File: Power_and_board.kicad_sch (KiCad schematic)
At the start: 24 parts, among them U4 AMS1117-5.0, U5 AMS1117-3.3

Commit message: initial rev of design
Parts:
- added C15, C16: 10uF, Capacitor_SMD:C_0805_2012Metric_Pad1.18x1.45mm_HandSolder, symbol Device:C
- added D6: SMF5V0A, Diode_SMD:D_SMF, symbol Diode:SMF5V0A
- added D7, D8: 1N5819WS, Diode_SMD:D_SOD-323_HandSoldering, symbol Device:D_Schottky
- C10, C7: LCSC (none) -> C49678
- C11, C5, C6, C8, C9: LCSC (none) -> C15850
- U4: LCSC (none) -> C6187
- U5: LCSC (none) -> C6186
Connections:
- net 12VDC IN: now also C15.1, D7.1 (K)
- net 3.3V: now also D8.2 (A)
- net Earth: now also C15.2, C16.2, D6.2 (A2)
- net VDD_5V: now also C16.1, D6.1 (A1), D7.2 (A), D8.1 (K)
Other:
- moved on the sheet: C10, C11, C5, C6, C7, C8, C9, D4, FID1, FID2, FID3, H1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

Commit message: library changes, fixed model for dc jack
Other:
- title: IoT LED Strip Driver -> Spotify Reactive IoT LED Strip Driver
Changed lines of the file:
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@@
   (paper "A4")
   (title_block
-    (title "IoT LED Strip Driver")
+    (title "Spotify Reactive IoT LED Strip Driver")
     (date "2023-08-13")
-    (rev "v1.0")
+    (rev "v1.8-a")
     (comment 1 "A modular, internet connected LED strip driver")
+    (comment 2 "that reacts to the currently playing song on spotify")
   )
   (junction (at 167.64 103.505) (diameter 0) (color 0 0 0 0)

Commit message: started work on new schematic
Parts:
- removed C10, C7: 100nF, Capacitor_SMD:C_0805_2012Metric_Pad1.18x1.45mm_HandSolder, symbol Device:C
- removed C11, C15, C16, C5, C6, C8, C9: 10uF, Capacitor_SMD:C_0805_2012Metric_Pad1.18x1.45mm_HandSolder, symbol Device:C
- removed D4: SMF18A, Diode_SMD:D_SMF, symbol Diode:SMF18A
- removed D5, D6: SMF5V0A, Diode_SMD:D_SMF, symbol Diode:SMF5V0A
- removed D7, D8: 1N5819WS, Diode_SMD:D_SOD-323_HandSoldering, symbol Device:D_Schottky
- removed FID1, FID2, FID3: Fiducial, Fiducial:Fiducial_0.5mm_Mask1mm, symbol Mechanical:Fiducial
- removed H1, H2, H3, H4: MountingHole_Pad, MountingHole:MountingHole_3.2mm_M3_Pad_Via, symbol Mechanical:MountingHole_Pad
- removed JP1: Jumper_2_Bridged, Connector_PinHeader_2.54mm:PinHeader_1x02_P2.54mm_Vertical, symbol Jumper:Jumper_2_Bridged
- removed JP2: USB PWR, Jumper:SolderJumper-2_P1.3mm_Open_RoundedPad1.0x1.5mm, symbol Jumper:SolderJumper_2_Open
- removed TP5: 12VDC, TestPoint:TestPoint_Pad_D2.0mm, symbol Connector:TestPoint
- removed TP6: 5V, TestPoint:TestPoint_Pad_D2.0mm, symbol Connector:TestPoint
- removed TP7: 3.3V, TestPoint:TestPoint_Pad_D2.0mm, symbol Connector:TestPoint
- removed TP8: GND, TestPoint:TestPoint_Pad_D2.0mm, symbol Connector:TestPoint
- removed U4: AMS1117-5.0, Package_TO_SOT_SMD:SOT-223-3_TabPin2, symbol Regulator_Linear:AMS1117-5.0
- removed U5: AMS1117-3.3, Package_TO_SOT_SMD:SOT-223-3_TabPin2, symbol Regulator_Linear:AMS1117-3.3
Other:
- note removed: "Power"

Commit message: schematic v1.9 initial rev
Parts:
- added C1, C8: 100nF, Capacitor_SMD:C_0805_2012Metric_Pad1.18x1.45mm_HandSolder, symbol Device:C
- added C6, C7, C9: 10uF, Capacitor_SMD:C_0805_2012Metric_Pad1.18x1.45mm_HandSolder, symbol Device:C
- added D2, D4: SMF5V0A, Diode_SMD:D_SMF, symbol Diode:SMF5V0A
- added D5: 1N5819WS, Diode_SMD:D_SOD-323_HandSoldering, symbol Device:D_Schottky
- added FID1, FID2, FID3: Fiducial, Fiducial:Fiducial_0.5mm_Mask1mm, symbol Mechanical:Fiducial
- added H1, H2, H3, H4: MountingHole_Pad, MountingHole:MountingHole_2.2mm_M2_Pad_Via, symbol Mechanical:MountingHole_Pad
- added JP1: Jumper_2_Bridged, Connector_PinHeader_2.54mm:PinHeader_1x02_P2.54mm_Vertical, symbol Jumper:Jumper_2_Bridged
- added JP2: USB PWR, Jumper:SolderJumper-2_P1.3mm_Open_RoundedPad1.0x1.5mm, symbol Jumper:SolderJumper_2_Open
- added TP3: 5V, TestPoint:TestPoint_Pad_D2.0mm, symbol Connector:TestPoint
- added TP4: 3.3V, TestPoint:TestPoint_Pad_D2.0mm, symbol Connector:TestPoint
- added TP5: GND, TestPoint:TestPoint_Pad_D2.0mm, symbol Connector:TestPoint
- added U1: AMS1117-3.3, Package_TO_SOT_SMD:SOT-223-3_TabPin2, symbol Regulator_Linear:AMS1117-3.3
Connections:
- new net 3.3V: C8.1, C9.1, D5.2 (A), TP4.1, U1.2 (VO)
- new net 5V: C1.1, C6.1, C7.1, D2.1 (A1), D4.1 (A1), D5.1 (K), JP1.1 (A), JP2.1 (A), TP3.1, U1.3 (VI)
- new net Earth: C1.2, C6.2, C7.2, C8.2, C9.2, D2.2 (A2), D4.2 (A2), H1.1, H2.1, H3.1, H4.1, TP5.1, U1.1 (GND)
- new net VBUS: JP1.2 (B), JP2.2 (B)

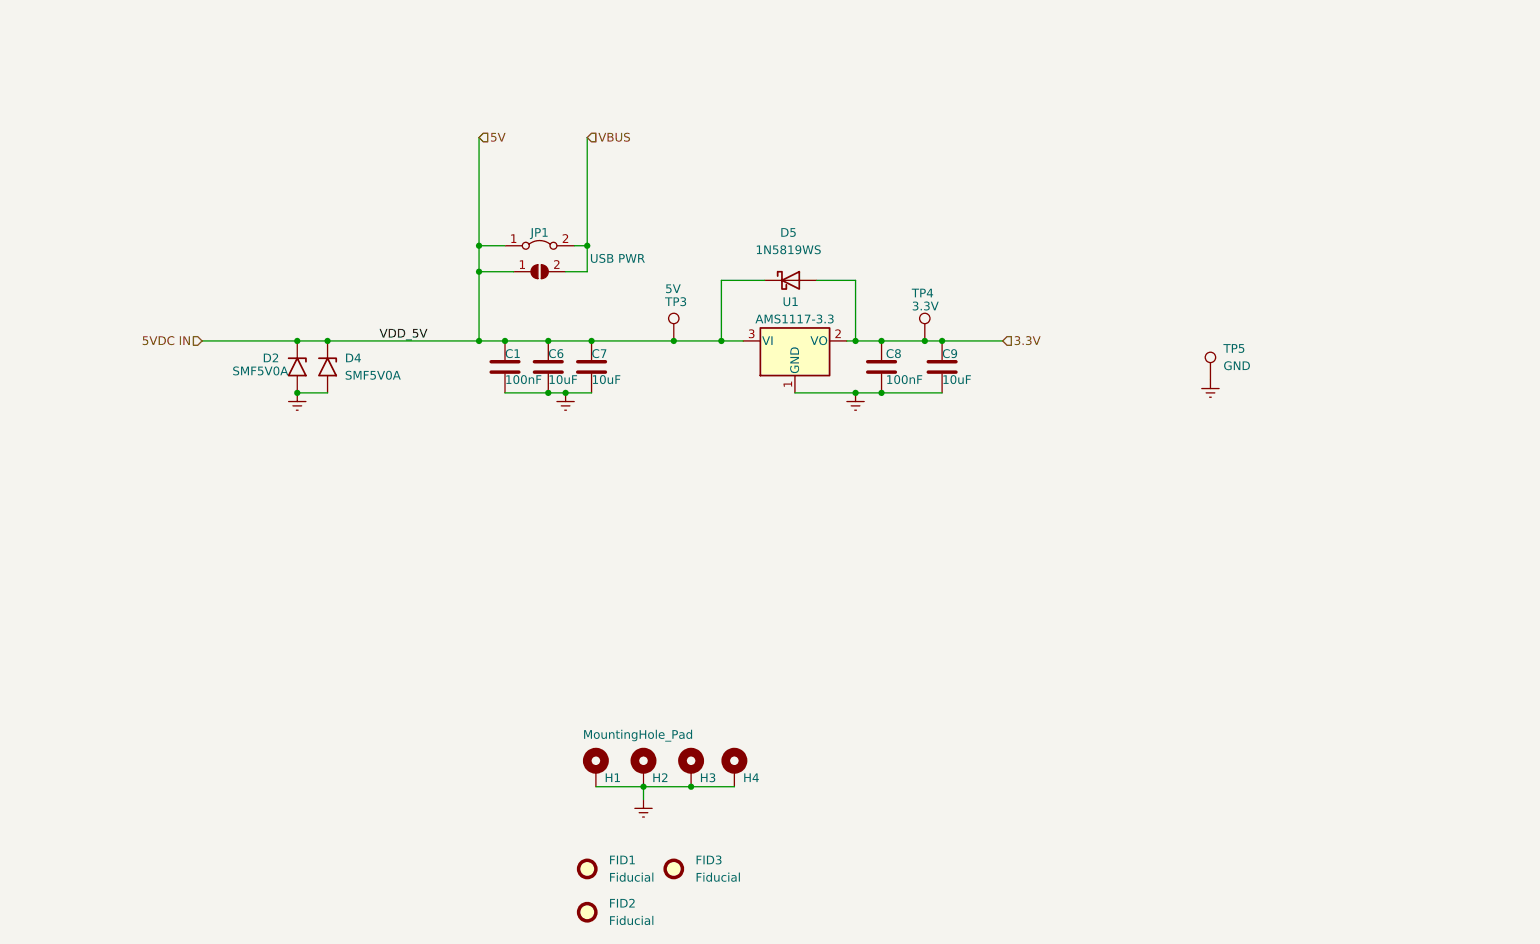
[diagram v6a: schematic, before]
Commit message: some small changes to schematic, cleaned up old pcb
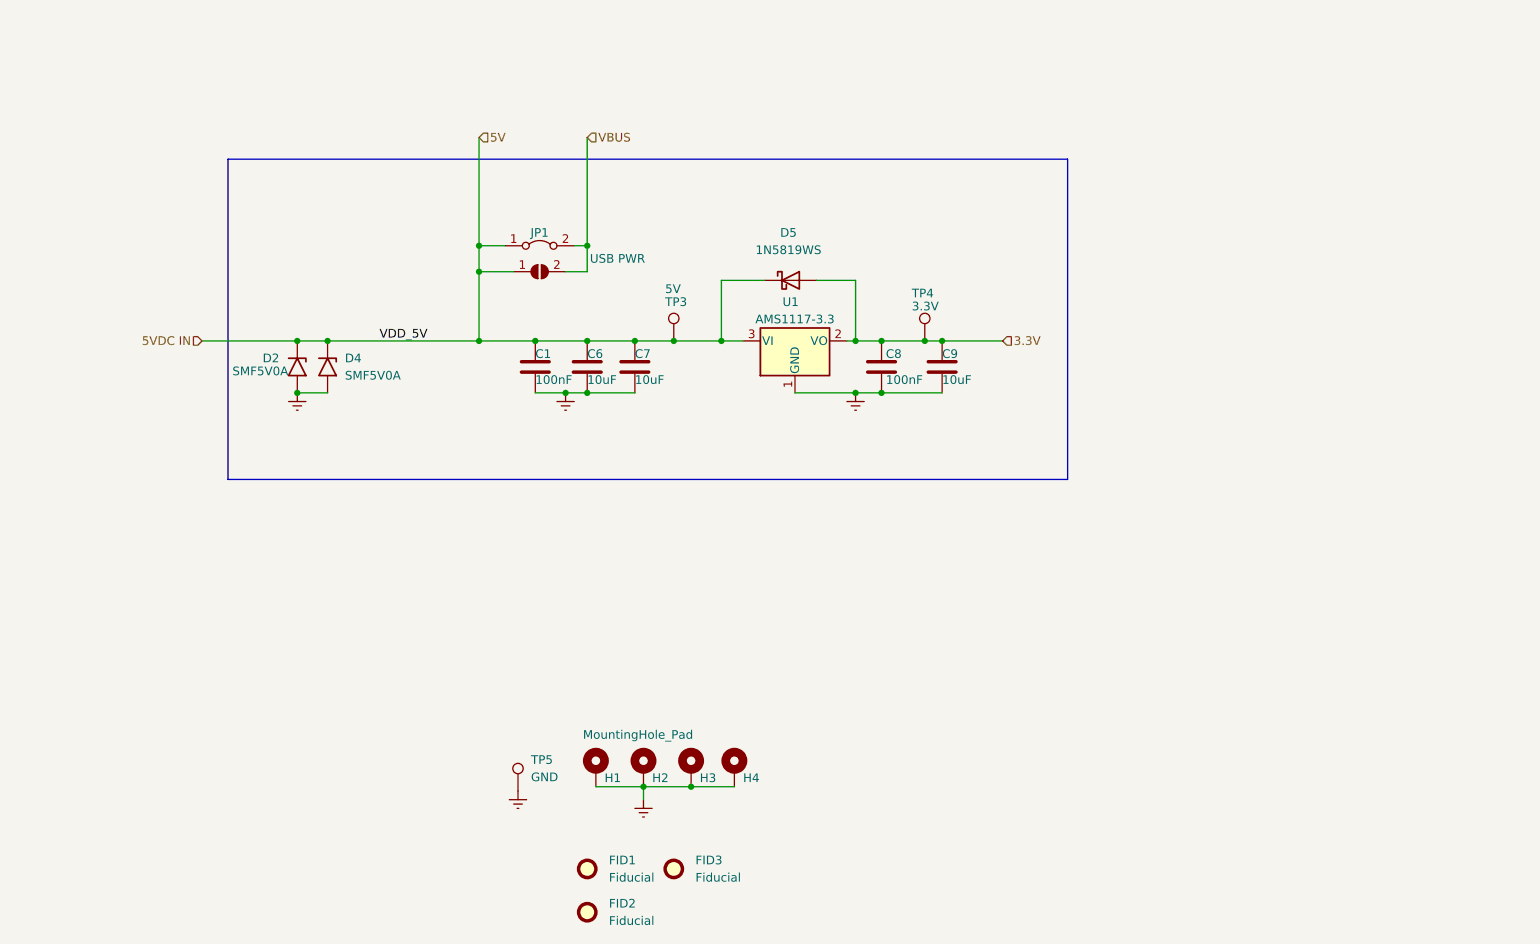
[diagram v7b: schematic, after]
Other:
- moved on the sheet: C1, C6, C7, TP5

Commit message: did layout, whoops
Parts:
- renumbered C6 to C2, C7 to C3, C8 to C4, C9 to C5, C1 to C6, D4 to D1, D5 to D3, FID3 to FID1, FID1 to FID2, FID2 to FID3, JP2 to JP3, JP1 to JP4, TP3 to TP1, TP4 to TP2, TP5 to TP3
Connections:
- net 5V renamed 5VDC IN
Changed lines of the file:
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@@
     (title "Spotify Reactive IoT LED Strip Driver")
     (date "2023-08-13")
-    (rev "v1.8-a")
+    (rev "v1.9.1-a")
     (comment 2 "to the currently playing song on spotify")
     (comment 3 "A modular, internet connected LED strip driver that reacts ")
@@
   (junction (at 124.46 90.17) (diameter 0) (color 0 0 0 0)
   )
-  (junction (at 124.46 86.36) (diameter 0) (color 0 0 0 0)
-  )
   (junction (at 140.335 86.36) (diameter 0) (color 0 0 0 0)
   )
@@
     (stroke (width 0) (type default))
   )
-  (wire (pts (xy 124.46 70.485) (xy 124.46 86.36))
-    (stroke (width 0) (type default))
-  )
   (wire (pts (xy 189.865 100.33) (xy 192.405 100.33))
     (stroke (width 0) (type default))
@@
     (stroke (width 0) (type default))
     (fill (type none))
-  )
-  (label "VDD_5V" (at 109.855 100.33 0) (fields_autoplaced)
-    (effects (font (size 1.27 1.27)) (justify left bottom))
   )
   (hierarchical_label "5VDC IN" (shape input) (at 83.82 100.33 180) (fields_autoplaced)
@@
   )
   (hierarchical_label "VBUS" (shape input) (at 140.335 70.485 0) (fields_autoplaced)
-    (effects (font (size 1.27 1.27)) (justify left))
-  )
-  (hierarchical_label "5V" (shape input) (at 124.46 70.485 0) (fields_autoplaced)
     (effects (font (size 1.27 1.27)) (justify left))
   )
@@
   (symbol (lib_id "Jumper:Jumper_2_Bridged") (at 133.35 86.36 0) (unit 1)
     (in_bom no) (on_board yes) (dnp no)
-    (property "Reference" "JP1" (at 133.35 84.455 0)
+    (property "Reference" "JP4" (at 133.35 84.455 0)
       (effects (font (size 1.27 1.27)))
     )
@@
       (project "iot_led_strip_pcb"
         (path "/745f5767-ebad-4719-b66e-073bc90db4bc/cfe13250-7fa5-4f24-964e-9463793dd38d"
-          (reference "JP1") (unit 1)
+          (reference "JP4") (unit 1)
         )
         (path "/745f5767-ebad-4719-b66e-073bc90db4bc"
@@
   (symbol (lib_id "Mechanical:Fiducial") (at 140.335 184.15 0) (unit 1)
     (in_bom no) (on_board yes) (dnp no) (fields_autoplaced)
-    (property "Reference" "FID2" (at 143.51 182.8799 0)
+    (property "Reference" "FID3" (at 143.51 182.8799 0)
       (effects (font (size 1.27 1.27)) (justify left))
     )
@@
       (project "iot_led_strip_pcb"
         (path "/745f5767-ebad-4719-b66e-073bc90db4bc/cfe13250-7fa5-4f24-964e-9463793dd38d"
-          (reference "FID2") (unit 1)
+          (reference "FID3") (unit 1)
         )
         (path "/745f5767-ebad-4719-b66e-073bc90db4bc"
@@
   (symbol (lib_id "Device:C") (at 192.405 104.14 0) (unit 1)
     (in_bom yes) (on_board yes) (dnp no)
-    (property "Reference" "C9" (at 192.405 102.235 0)
+    (property "Reference" "C5" (at 192.405 102.235 0)
       (effects (font (size 1.27 1.27)) (justify left))
     )
@@
       (project "iot_led_strip_pcb"
         (path "/745f5767-ebad-4719-b66e-073bc90db4bc/cfe13250-7fa5-4f24-964e-9463793dd38d"
-          (reference "C9") (unit 1)
+          (reference "C5") (unit 1)
         )
         (path "/745f5767-ebad-4719-b66e-073bc90db4bc"
@@
   (symbol (lib_id "Device:C") (at 147.32 104.14 0) (unit 1)
     (in_bom yes) (on_board yes) (dnp no)
-    (property "Reference" "C7" (at 147.32 102.235 0)
+    (property "Reference" "C3" (at 147.32 102.235 0)
       (effects (font (size 1.27 1.27)) (justify left))
     )
@@
       (project "iot_led_strip_pcb"
         (path "/745f5767-ebad-4719-b66e-073bc90db4bc/cfe13250-7fa5-4f24-964e-9463793dd38d"
-          (reference "C7") (unit 1)
+          (reference "C3") (unit 1)
         )
         (path "/745f5767-ebad-4719-b66e-073bc90db4bc"
@@
   (symbol (lib_id "Connector:TestPoint") (at 153.035 100.33 0) (unit 1)
     (in_bom no) (on_board yes) (dnp no)
-    (property "Reference" "TP3" (at 151.765 94.615 0)
+    (property "Reference" "TP1" (at 151.765 94.615 0)
       (effects (font (size 1.27 1.27)) (justify left))
     )
@@
       (project "iot_led_strip_pcb"
         (path "/745f5767-ebad-4719-b66e-073bc90db4bc/cfe13250-7fa5-4f24-964e-9463793dd38d"
-          (reference "TP3") (unit 1)
+          (reference "TP1") (unit 1)
         )
         (path "/745f5767-ebad-4719-b66e-073bc90db4bc"
@@
   (symbol (lib_id "Device:C") (at 140.335 104.14 0) (unit 1)
     (in_bom yes) (on_board yes) (dnp no)
-    (property "Reference" "C6" (at 140.335 102.235 0)
+    (property "Reference" "C2" (at 140.335 102.235 0)
       (effects (font (size 1.27 1.27)) (justify left))
     )
@@
       (project "iot_led_strip_pcb"
         (path "/745f5767-ebad-4719-b66e-073bc90db4bc/cfe13250-7fa5-4f24-964e-9463793dd38d"
-          (reference "C6") (unit 1)
+          (reference "C2") (unit 1)
         )
         (path "/745f5767-ebad-4719-b66e-073bc90db4bc"
@@
   (symbol (lib_id "Diode:SMF5V0A") (at 102.235 104.14 270) (unit 1)
     (in_bom yes) (on_board yes) (dnp no) (fields_autoplaced)
-    (property "Reference" "D4" (at 104.775 102.8699 90)
+    (property "Reference" "D1" (at 104.775 102.8699 90)
       (effects (font (size 1.27 1.27)) (justify left))
     )
@@
       (project "iot_led_strip_pcb"
         (path "/745f5767-ebad-4719-b66e-073bc90db4bc/cfe13250-7fa5-4f24-964e-9463793dd38d"
-          (reference "D4") (unit 1)
+          (reference "D1") (unit 1)
         )
         (path "/745f5767-ebad-4719-b66e-073bc90db4bc"
@@
   (symbol (lib_id "Mechanical:Fiducial") (at 140.335 177.8 0) (unit 1)
     (in_bom no) (on_board yes) (dnp no) (fields_autoplaced)
-    (property "Reference" "FID1" (at 143.51 176.5299 0)
+    (property "Reference" "FID2" (at 143.51 176.5299 0)
       (effects (font (size 1.27 1.27)) (justify left))
     )
@@
       (project "iot_led_strip_pcb"
         (path "/745f5767-ebad-4719-b66e-073bc90db4bc/cfe13250-7fa5-4f24-964e-9463793dd38d"
-          (reference "FID1") (unit 1)
+          (reference "FID2") (unit 1)
         )
         (path "/745f5767-ebad-4719-b66e-073bc90db4bc"
@@
   (symbol (lib_id "Mechanical:Fiducial") (at 153.035 177.8 0) (unit 1)
     (in_bom no) (on_board yes) (dnp no) (fields_autoplaced)
-    (property "Reference" "FID3" (at 156.21 176.5299 0)
+    (property "Reference" "FID1" (at 156.21 176.5299 0)
       (effects (font (size 1.27 1.27)) (justify left))
     )
@@
       (project "iot_led_strip_pcb"
         (path "/745f5767-ebad-4719-b66e-073bc90db4bc/cfe13250-7fa5-4f24-964e-9463793dd38d"
-          (reference "FID3") (unit 1)
+          (reference "FID1") (unit 1)
         )
         (path "/745f5767-ebad-4719-b66e-073bc90db4bc"
@@
   (symbol (lib_id "Connector:TestPoint") (at 130.175 166.37 0) (unit 1)
     (in_bom no) (on_board yes) (dnp no) (fields_autoplaced)
-    (property "Reference" "TP5" (at 132.08 161.7979 0)
+    (property "Reference" "TP3" (at 132.08 161.7979 0)
       (effects (font (size 1.27 1.27)) (justify left))
     )
@@
       (project "iot_led_strip_pcb"
         (path "/745f5767-ebad-4719-b66e-073bc90db4bc/cfe13250-7fa5-4f24-964e-9463793dd38d"
-          (reference "TP5") (unit 1)
+          (reference "TP3") (unit 1)
         )
         (path "/745f5767-ebad-4719-b66e-073bc90db4bc"
@@
   (symbol (lib_id "Device:C") (at 132.715 104.14 0) (unit 1)
     (in_bom yes) (on_board yes) (dnp no)
-    (property "Reference" "C1" (at 132.715 102.235 0)
+    (property "Reference" "C6" (at 132.715 102.235 0)
       (effects (font (size 1.27 1.27)) (justify left))
     )
@@
       (project "iot_led_strip_pcb"
         (path "/745f5767-ebad-4719-b66e-073bc90db4bc/cfe13250-7fa5-4f24-964e-9463793dd38d"
-          (reference "C1") (unit 1)
+          (reference "C6") (unit 1)
         )
         (path "/745f5767-ebad-4719-b66e-073bc90db4bc"
@@
   (symbol (lib_id "Jumper:SolderJumper_2_Open") (at 133.35 90.17 0) (unit 1)
     (in_bom no) (on_board yes) (dnp no)
-    (property "Reference" "JP2" (at 132.08 92.71 0)
+    (property "Reference" "JP3" (at 132.08 92.71 0)
       (effects (font (size 1.27 1.27)) hide)
     )
@@
       (project "iot_led_strip_pcb"
         (path "/745f5767-ebad-4719-b66e-073bc90db4bc/cfe13250-7fa5-4f24-964e-9463793dd38d"
-          (reference "JP2") (unit 1)
+          (reference "JP3") (unit 1)
         )
         (path "/745f5767-ebad-4719-b66e-073bc90db4bc"
@@
   (symbol (lib_id "Device:D_Schottky") (at 170.18 91.44 0) (unit 1)
     (in_bom yes) (on_board yes) (dnp no) (fields_autoplaced)
-    (property "Reference" "D5" (at 169.8625 84.455 0)
+    (property "Reference" "D3" (at 169.8625 84.455 0)
       (effects (font (size 1.27 1.27)))
     )
@@
       (project "iot_led_strip_pcb"
         (path "/745f5767-ebad-4719-b66e-073bc90db4bc/cfe13250-7fa5-4f24-964e-9463793dd38d"
-          (reference "D5") (unit 1)
+          (reference "D3") (unit 1)
         )
         (path "/745f5767-ebad-4719-b66e-073bc90db4bc"
@@
   (symbol (lib_id "Device:C") (at 183.515 104.14 0) (unit 1)
     (in_bom yes) (on_board yes) (dnp no)
-    (property "Reference" "C8" (at 184.15 102.235 0)
+    (property "Reference" "C4" (at 184.15 102.235 0)
       (effects (font (size 1.27 1.27)) (justify left))
     )
@@
       (project "iot_led_strip_pcb"
         (path "/745f5767-ebad-4719-b66e-073bc90db4bc/cfe13250-7fa5-4f24-964e-9463793dd38d"
-          (reference "C8") (unit 1)
+          (reference "C4") (unit 1)
         )
         (path "/745f5767-ebad-4719-b66e-073bc90db4bc"
@@
   (symbol (lib_id "Connector:TestPoint") (at 189.865 100.33 0) (unit 1)
     (in_bom no) (on_board yes) (dnp no)
-    (property "Reference" "TP4" (at 187.96 93.345 0)
+    (property "Reference" "TP2" (at 187.96 93.345 0)
       (effects (font (size 1.27 1.27)) (justify left))
     )
@@
       (project "iot_led_strip_pcb"
         (path "/745f5767-ebad-4719-b66e-073bc90db4bc/cfe13250-7fa5-4f24-964e-9463793dd38d"
-          (reference "TP4") (unit 1)
-        )
-        (path "/745f5767-ebad-4719-b66e-073bc90db4bc"
+          (reference "TP2") (unit 1)
+        )
+        (path "/745f5767-ebad-4719-b66e-073bc90db4bc"
